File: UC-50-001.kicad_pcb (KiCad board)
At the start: 2 copper layers, 283 x 177.5 mm, 255 parts, among them J01 Jumper Wire, J02 Jumper Wire, J03 Jumper wire, J04 Jumper wire, J05 Jumper Wire, J07 Jumper wire, P01 1K, P02 ?, Q01 16MHz, T01 BC547B, T02 BC547B, T03 BC547B, T04 BC557B, T05 BC547B, T06 BC547B, T07 BC547B, T08 BC557B, T09 BC547B, T10 BC547B, T11 BC547B, T12 BDX54, T13 BC547B

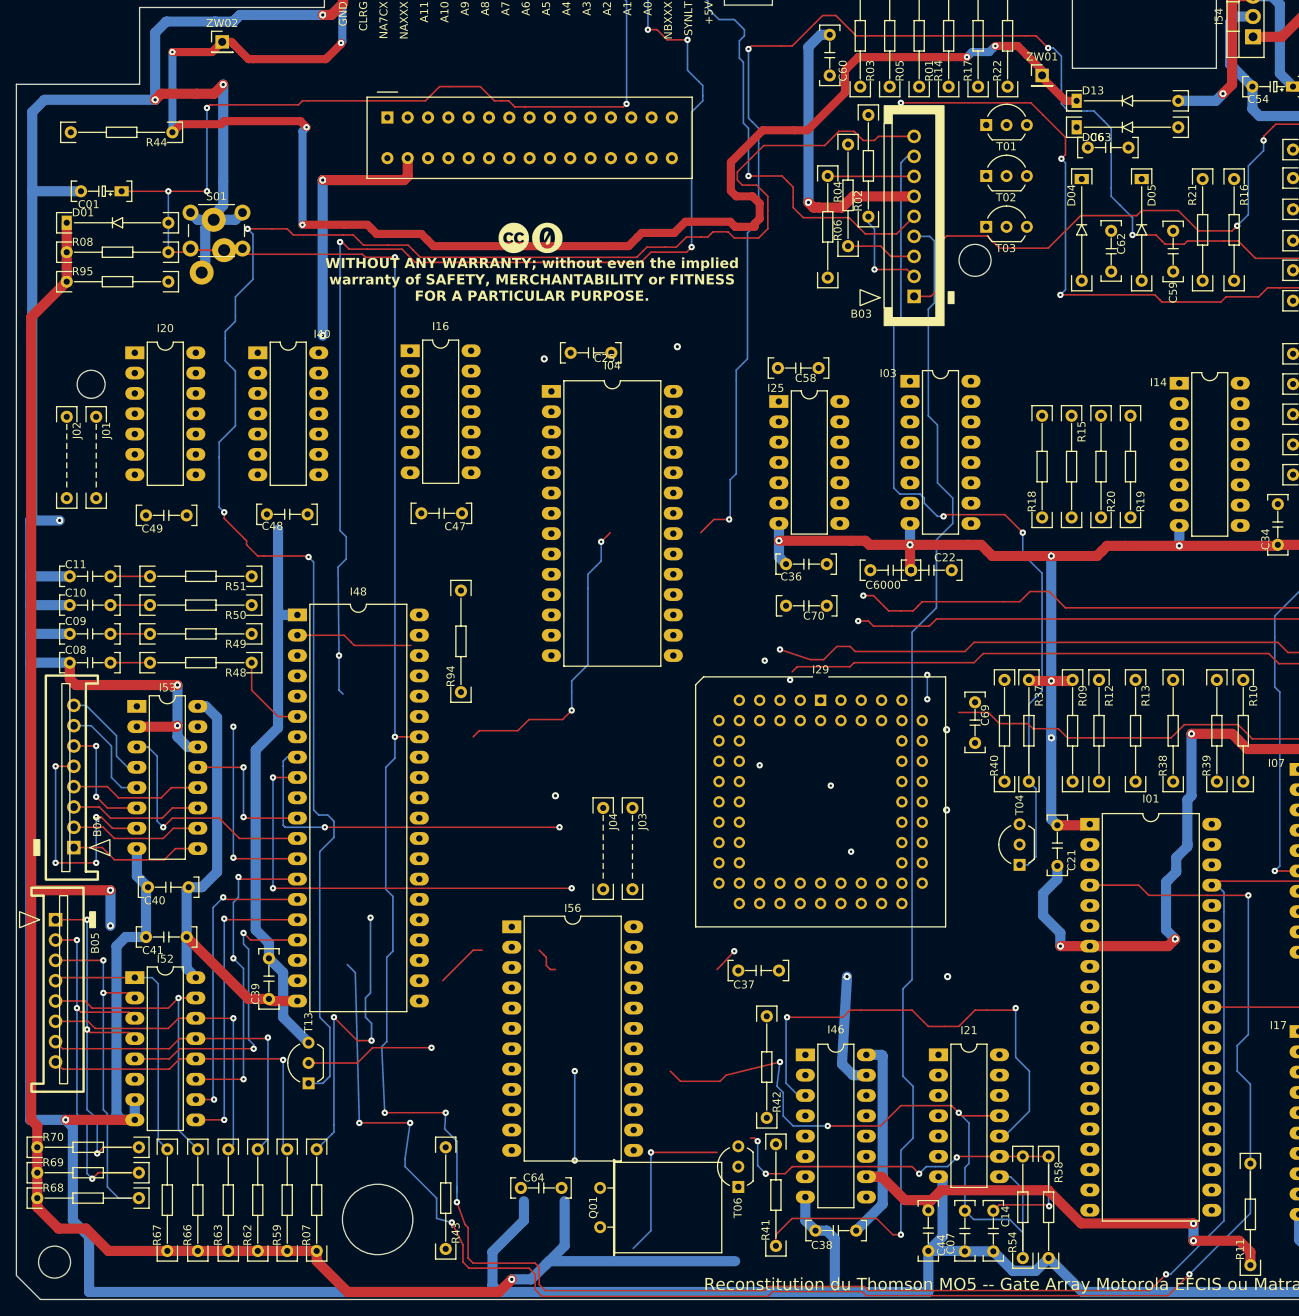
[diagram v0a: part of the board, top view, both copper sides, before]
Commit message: [pcb] area A.2, A.3
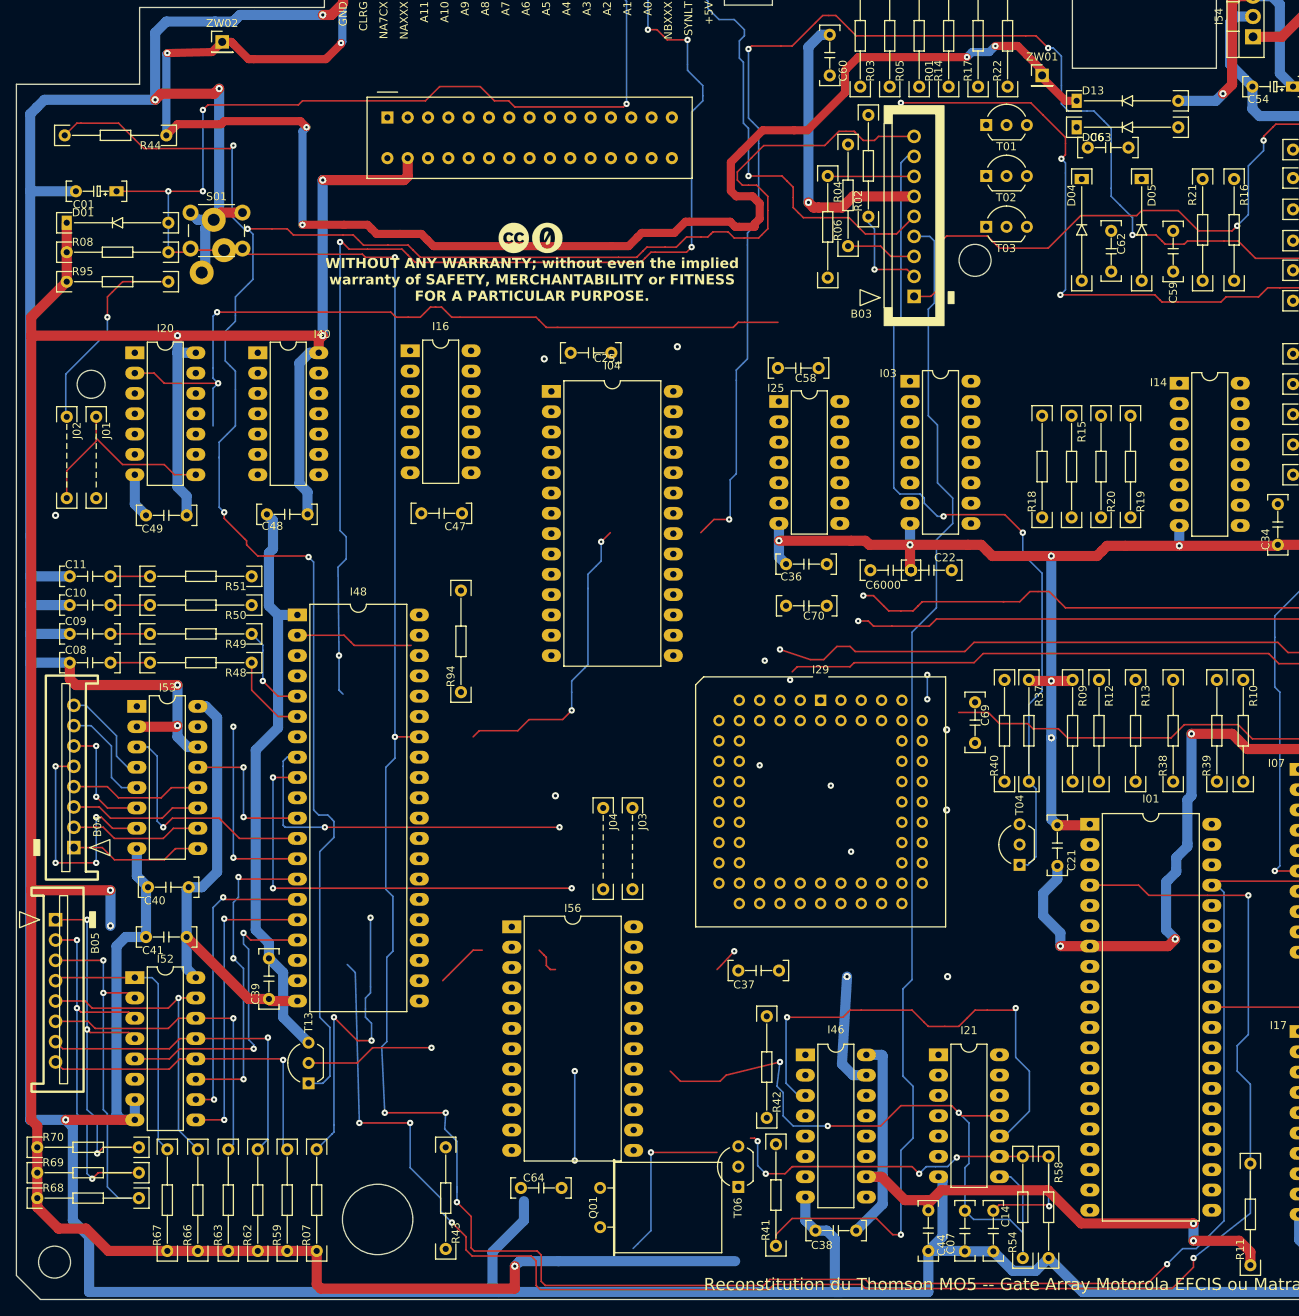
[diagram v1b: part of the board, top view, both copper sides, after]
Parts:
- moved R44 0.85 mm to (72.4, 94.5)
- moved C01 0.63 mm to (70.0, 101.5)
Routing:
- net ADDR12: track 0.00 -> 98.1 mm, vias 0 -> 2
- net +5V: track 1576.3 -> 1656.7 mm, vias 32 -> 33
- net CLTV: track 226.8 -> 261.5 mm, vias 3 -> 4
- net Net-(I20-3Y): track 0.00 -> 26.2 mm
- net B/NBXXX: track 0.00 -> 25.6 mm, vias 0 -> 1
- net Net-(I48-PA3): track 0.00 -> 11.6 mm, vias 0 -> 1
- net GND: track 1942.8 -> 1945.9 mm
- net +12V: track 200.8 -> 202.7 mm
- net I/~{FIRQ}: track 364.1 -> 362.5 mm
